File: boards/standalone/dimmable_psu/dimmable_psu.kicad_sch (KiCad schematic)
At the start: 81 parts, among them J1 DIM_IN, J2 PWM_IN, J3 POWER, J4 POWER_OUT, Q1 2N7002, Q2 IRF540N, Q3 IRF540N, SW1 SW_DIP_SPLIT_x02, U1 LM324, U2 LMC7660, U3 TPS92640

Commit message: rework dimmable_psu opamp power supplies
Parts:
- removed D1, D2, D3, D4: D_Schottky_Trans, Diode_SMD:D_SOD-123, symbol Device:D_Schottky
- removed D6: 15v, Diode_THT:D_DO-15_P12.70mm_Horizontal, symbol Device:D_Zener
- removed D9: 2.7v, Diode_THT:D_DO-15_P12.70mm_Horizontal, symbol Device:D_Zener
- removed U3: TPS92640, Package_SO:HTSSOP-14-1EP_4.4x5mm_P0.65mm_EP3.4x5mm_Mask3x3.1mm, symbol ti_reg:TPS92640
- added C4, C5: 100n, Capacitor_SMD:C_0805_2012Metric_Pad1.18x1.45mm_HandSolder, symbol Device:C
- added D1, D2: BAT54S, Package_TO_SOT_SMD:SOT-23, symbol Diode:BAT54S
- added R17: 47k, Resistor_SMD:R_0805_2012Metric_Pad1.20x1.40mm_HandSolder, symbol Device:R
- added R21: 59k, Resistor_SMD:R_0805_2012Metric_Pad1.20x1.40mm_HandSolder, symbol Device:R
- added U2: AP2205-ADJ, Package_TO_SOT_SMD:SOT-23-5, symbol Regulator_Linear:AP2204K-ADJ
- added U3: MAX17651, Package_TO_SOT_SMD:TSOT-23-6, symbol reg:MAX17651
- added U5: TPS92640, Package_SO:HTSSOP-14-1EP_4.4x5mm_P0.65mm_EP3.4x5mm_Mask3x3.1mm, symbol reg:TPS92640
- R16: value 1.2k -> 47k; footprint Resistor_THT:R_Axial_DIN0309_L9.0mm_D3.2mm_P12.70mm_Horizontal -> Resistor_SMD:R_0805_2012Metric_Pad1.20x1.40mm_HandSolder
- R2: renamed from R1; value 47k -> 22k
- R20: renamed from R8; value 750 -> 1.5M; footprint Resistor_THT:R_Axial_DIN0309_L9.0mm_D3.2mm_P12.70mm_Horizontal -> Resistor_SMD:R_0805_2012Metric_Pad1.20x1.40mm_HandSolder
- renumbered C2 to C1, C9 to C10, C10 to C11, C5 to C12, C11 to C13, C12 to C14, C13 to C15, C14 to C16, C15 to C17, C16 to C18, C17 to C19, C3 to C2, C18 to C20, C1 to C3, C4 to C9, D5 to D3, D7 to D4, D8 to D5, D10 to D6, R29 to R1, R17 to R18, R18 to R19, R19 to R22, R20 to R23, R21 to R24, R22 to R25, R23 to R26, R24 to R27, R25 to R28, R26 to R29, R2 to R3, R27 to R30, R28 to R31, R3 to R4, R4 to R5, R5 to R6, R6 to R7, R7 to R8, TP5 to TP4, TP6 to TP5, TP4 to TP6, U2 to U4
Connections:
- net CSENSE: now also U5.9 (CSENSE)
- net DIM_IN: now also D1.3
- net GND: now also C4.2, C5.2, D1.1, D2.1, R17.2, R21.2, U2.2 (GND), U3.2 (GND), U5.15 (TP), U5.8 (GND)
- net IADJ: now also U5.6 (IADJ)
- net POWER_JUN: now also U5.13 (SW)
- net PWM_IN: now also D2.3
- net UDIM: now also U5.3 (UDIM)
- net VDD: now also R20.1, C4.1, D1.2, D2.2, U2.1 (VIN), U2.3 (EN), U3.4 (OUT); no longer R20.2
- net VNEGREF: now also R16.1, U2.5 (VOUT); no longer R16.2
- net VOUT_SENSE: now also U5.4 (VOUT)
- net VPP: now also C5.1, U3.1 (EN), U3.3 (VIN), U5.1 (VIN); no longer R16.1, R20.1
- net VREF: now also U5.5 (VREF)
- net at R26.1: now also U5.10 (LG)
- net at C19.1, D6.2 (A): now also U5.11 (VCC)
- net at C18.2, D6.1 (K): now also U5.12 (BOOT)
- net at R25.1: now also U5.14 (HG)
- net at C13.1, R24.2: now also U5.2 (RON)
- net at C16.1: now also U5.7 (COMP)
- new net: R20.2, R21.1, U3.6 (FB)
- new net: R16.2, R17.1, U2.4 (ADJ)
- no-connect marks 4 -> 5
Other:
- moved on the sheet: C1, C12, C2, C6, C7, C9, R20, TP6

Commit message: dimmable psu pcb almost finished
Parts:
- added C3, C?: 100n, Capacitor_SMD:C_0805_2012Metric_Pad1.18x1.45mm_HandSolder, symbol Device:C
- renumbered C9 to C10, C10 to C11, C11 to C12, C12 to C13, C13 to C14, C14 to C15, C15 to C16, C16 to C17, C17 to C18, C18 to C19, C19 to C20, C20 to C21, C3 to C4, C4 to C5, C5 to C6, C6 to C7, C7 to C8, C8 to C9
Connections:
- net GND: now also C3.2, C?.2
- net UDIM: no longer TP5.1
- net UDIM_OFF: now also TP5.1
- net VDD: now also C?.1
- net VPP: now also C3.1
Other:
- moved on the sheet: TP5

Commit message: add filled areas and make some cosmetic fixes
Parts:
- gave numbers to parts that had none: 1
- renumbered C9 to C10, C10 to C11, C11 to C12, C12 to C13, C13 to C14, C14 to C15, C15 to C16, C16 to C17, C17 to C18, C18 to C19, C19 to C20, C20 to C21, C21 to C22, C4 to C5, C5 to C6, C6 to C7, C7 to C8, C8 to C9, TP5 to TP4, TP4 to TP5

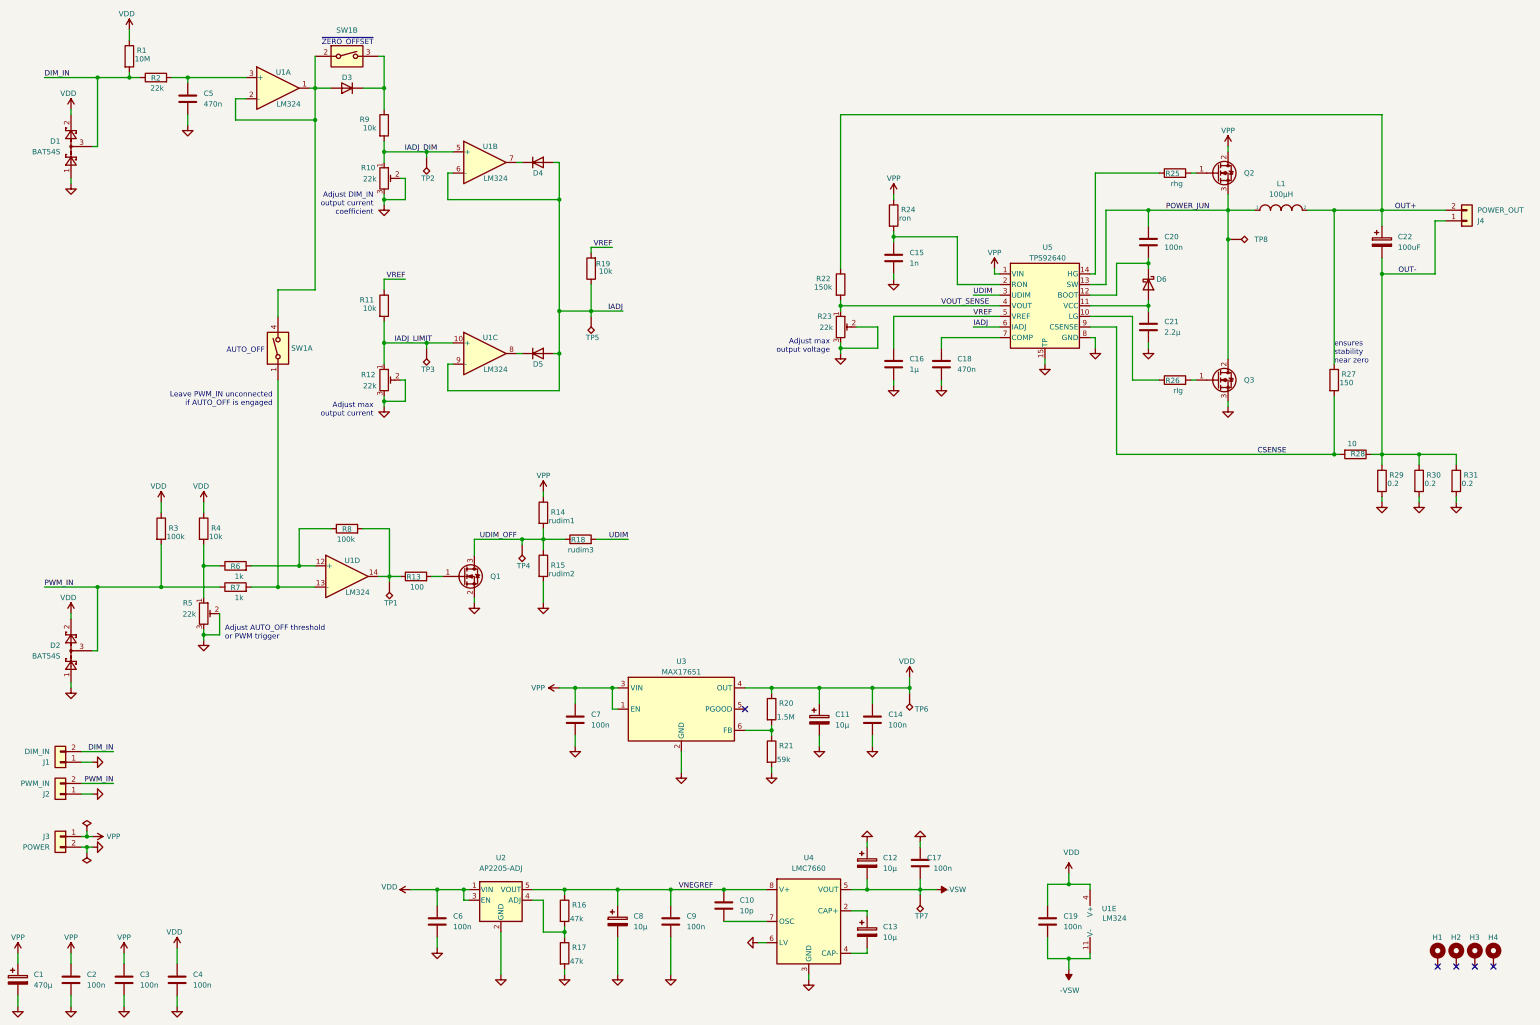
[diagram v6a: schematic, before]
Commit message: replace LDOs with npns
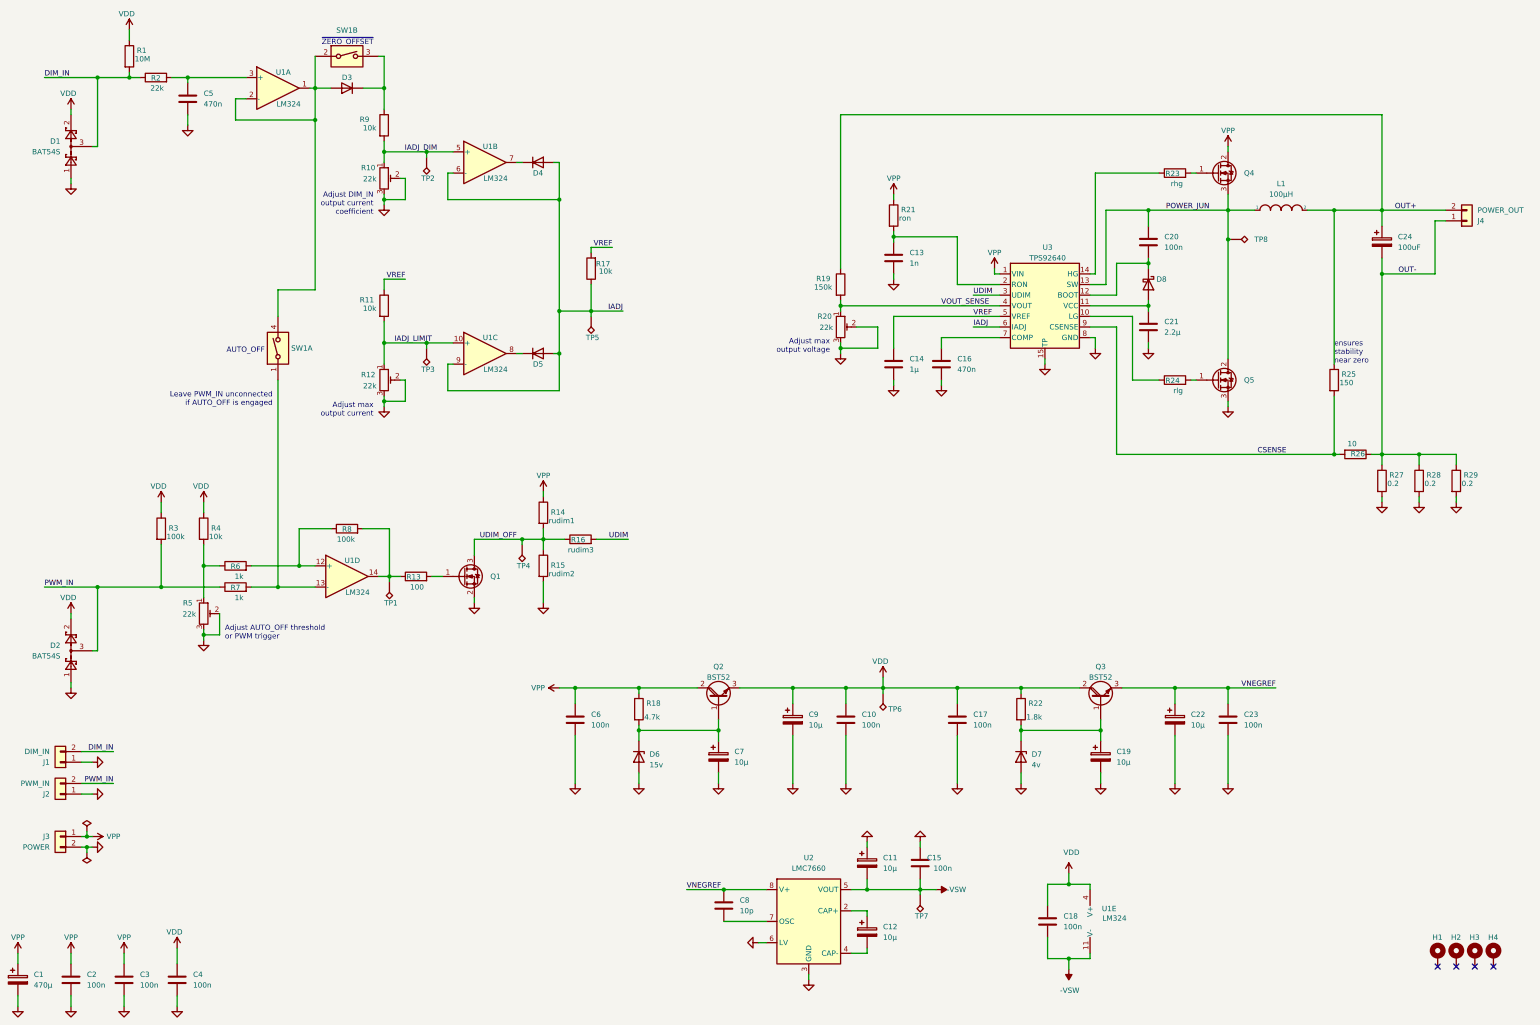
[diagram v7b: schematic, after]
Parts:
- removed C13, C8: 10µ, Capacitor_SMD:CP_Elec_5x5.4, symbol Device:C_Polarized
- removed C6, C9: 100n, Capacitor_SMD:C_0805_2012Metric_Pad1.18x1.45mm_HandSolder, symbol Device:C
- removed R16, R17: 47k, Resistor_SMD:R_0805_2012Metric_Pad1.20x1.40mm_HandSolder, symbol Device:R
- removed R20: 1.5M, Resistor_SMD:R_0805_2012Metric_Pad1.20x1.40mm_HandSolder, symbol Device:R
- removed R21: 59k, Resistor_SMD:R_0805_2012Metric_Pad1.20x1.40mm_HandSolder, symbol Device:R
- removed U2: AP2205-ADJ, Package_TO_SOT_SMD:SOT-23-5, symbol Regulator_Linear:AP2204K-ADJ
- removed U3: MAX17651, Package_TO_SOT_SMD:TSOT-23-6, symbol reg:MAX17651
- added C17, C23: 100n, Capacitor_SMD:C_0805_2012Metric_Pad1.18x1.45mm_HandSolder, symbol Device:C
- added C19, C22, C7, C9: 10µ, Capacitor_SMD:C_1206_3216Metric_Pad1.33x1.80mm_HandSolder, symbol Device:C_Polarized
- added D6: 15v, Diode_SMD:D_SOD-323_HandSoldering, symbol Device:D_Zener
- added D7: 4v, Diode_SMD:D_SOD-323_HandSoldering, symbol Device:D_Zener
- added Q2, Q3: BST52, Package_TO_SOT_SMD:SOT-89-3, symbol Transistor_BJT:BCV49
- added R18: 4.7k, Resistor_SMD:R_0805_2012Metric_Pad1.20x1.40mm_HandSolder, symbol Device:R
- added R22: 1.8k, Resistor_SMD:R_0805_2012Metric_Pad1.20x1.40mm_HandSolder, symbol Device:R
- C11, C12: footprint Capacitor_SMD:CP_Elec_5x5.4 -> Capacitor_SMD:C_1206_3216Metric_Pad1.33x1.80mm_HandSolder; shop https://store.comet.bg/Catalogue/Product/29567/ -> https://store.comet.bg/Catalogue/Product/5162150/
- renumbered C14 to C10, C15 to C13, C16 to C14, C17 to C15, C18 to C16, C19 to C18, C22 to C24, C7 to C6, C10 to C8, D6 to D8, Q2 to Q4, Q3 to Q5, R18 to R16, R19 to R17, R22 to R19, R23 to R20, R24 to R21, R25 to R23, R26 to R24, R27 to R25, R28 to R26, R29 to R27, R30 to R28, R31 to R29, U4 to U2, U5 to U3
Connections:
- net -VSW: now also C11.2; no longer C12.2
- net GND: now also C11.1, C17.2, C19.2, C22.2, C23.2, C7.2, C9.2, D6.2 (A), D7.2 (A); no longer C11.2, C12.1
- net VDD: now also C17.1, C9.1, Q2.3 (E), Q3.2 (C), R22.1; no longer C11.1
- net VNEGREF: now also C22.1, C23.1, Q3.3 (E)
- net VPP: now also Q2.2 (C), R18.1
- net at U2.2 (CAP+): now also C12.1
- net at U2.4 (CAP-): now also C12.2
- new net: C19.1, D7.1 (K), Q3.1 (B), R22.2
- new net: C7.1, D6.1 (K), Q2.1 (B), R18.2
- no-connect marks 5 -> 4
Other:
- moved on the sheet: C10, TP6

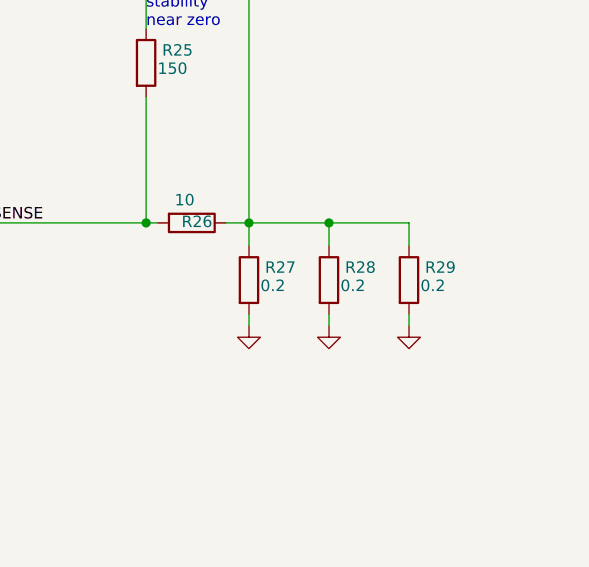
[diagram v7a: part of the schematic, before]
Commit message: use 1206 power resistors
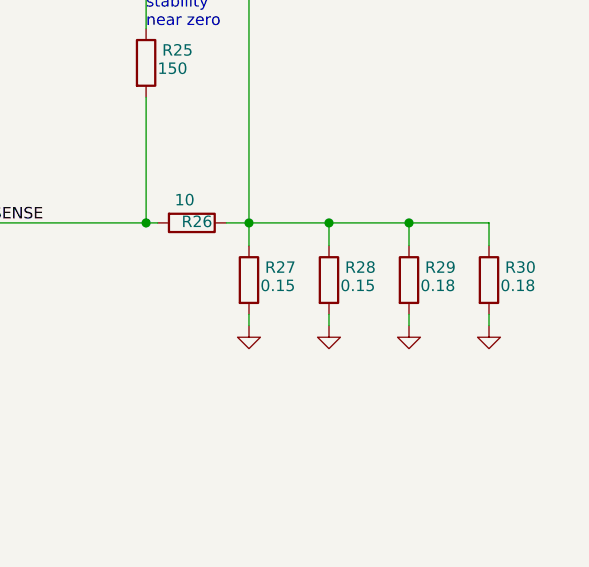
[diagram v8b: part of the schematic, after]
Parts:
- added R30: 0.18, Resistor_SMD:R_1206_3216Metric_Pad1.30x1.75mm_HandSolder, symbol Device:R
- R25, R26: footprint Resistor_THT:R_Axial_DIN0309_L9.0mm_D3.2mm_P12.70mm_Horizontal -> Resistor_SMD:R_1206_3216Metric_Pad1.30x1.75mm_HandSolder
- R27, R28: value 0.2 -> 0.15; footprint Resistor_THT:R_Axial_DIN0309_L9.0mm_D3.2mm_P12.70mm_Horizontal -> Resistor_SMD:R_1206_3216Metric_Pad1.30x1.75mm_HandSolder
- R29: value 0.2 -> 0.18; footprint Resistor_THT:R_Axial_DIN0309_L9.0mm_D3.2mm_P12.70mm_Horizontal -> Resistor_SMD:R_1206_3216Metric_Pad1.30x1.75mm_HandSolder
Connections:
- net GND: now also R30.2
- net OUT-: now also R30.1
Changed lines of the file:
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@@
-(kicad_sch (version 20210126) (generator eeschema)
+(kicad_sch (version 20210406) (generator eeschema)
   (paper "A3")
   (title_block
@@
   (junction (at 359.41 135.89) (diameter 1.016) (color 0 0 0 0))
   (junction (at 368.3 135.89) (diameter 1.016) (color 0 0 0 0))
+  (junction (at 377.19 135.89) (diameter 1.016) (color 0 0 0 0))
   (no_connect (at 372.745 258.445))
   (no_connect (at 377.19 258.445))
@@
     (stroke (width 0) (type solid) (color 0 0 0 0))
   )
+  (wire (pts (xy 386.08 135.89) (xy 377.19 135.89))
+    (stroke (width 0) (type solid) (color 0 0 0 0))
+  )
+  (wire (pts (xy 386.08 138.43) (xy 386.08 135.89))
+    (stroke (width 0) (type solid) (color 0 0 0 0))
+  )
+  (wire (pts (xy 386.08 146.05) (xy 386.08 147.32))
+    (stroke (width 0) (type solid) (color 0 0 0 0))
+  )
   (text "Adjust AUTO_OFF threshold\nor PWM trigger" (at 82.55 180.34 0)
     (effects (font (size 1.27 1.27)) (justify left bottom))
@@
     (pin "1")
   )
+  (symbol (lib_id "power:GND") (at 386.08 147.32 0) (unit 1)
+    (in_bom yes) (on_board yes)
+    (property "Reference" "#PWR060" (id 0) (at 386.08 153.67 0)
+      (effects (font (size 1.27 1.27)) hide)
+    )
+    (property "Value" "GND" (id 1) (at 386.715 152.4 0)
+      (effects (font (size 1.27 1.27)) hide)
+    )
+    (property "Footprint" "" (id 2) (at 386.08 147.32 0)
+      (effects (font (size 1.27 1.27)) hide)
+    )
+    (property "Datasheet" "" (id 3) (at 386.08 147.32 0)
+      (effects (font (size 1.27 1.27)) hide)
+    )
+    (pin "1")
+  )
   (symbol (lib_id "Amplifier_Operational:LM324") (at 292.1 247.65 0) (unit 5)
     (in_bom yes) (on_board yes)
@@
       (effects (font (size 1.27 1.27)) (justify left))
     )
-    (property "Footprint" "Resistor_THT:R_Axial_DIN0309_L9.0mm_D3.2mm_P12.70mm_Horizontal" (id 2) (at 346.202 118.11 90)
+    (property "Footprint" "Resistor_SMD:R_1206_3216Metric_Pad1.30x1.75mm_HandSolder" (id 2) (at 346.202 118.11 90)
       (effects (font (size 1.27 1.27)) hide)
     )
@@
       (effects (font (size 1.27 1.27)) (justify left))
     )
-    (property "Footprint" "Resistor_THT:R_Axial_DIN0309_L9.0mm_D3.2mm_P12.70mm_Horizontal" (id 2) (at 353.06 134.112 90)
+    (property "Footprint" "Resistor_SMD:R_1206_3216Metric_Pad1.30x1.75mm_HandSolder" (id 2) (at 353.06 134.112 90)
       (effects (font (size 1.27 1.27)) hide)
     )
@@
       (effects (font (size 1.27 1.27)) (justify left))
     )
-    (property "Value" "0.2" (id 1) (at 360.68 142.875 0)
+    (property "Value" "0.15" (id 1) (at 360.68 142.875 0)
       (effects (font (size 1.27 1.27)) (justify left))
     )
-    (property "Footprint" "Resistor_THT:R_Axial_DIN0309_L9.0mm_D3.2mm_P12.70mm_Horizontal" (id 2) (at 357.632 142.24 90)
+    (property "Footprint" "Resistor_SMD:R_1206_3216Metric_Pad1.30x1.75mm_HandSolder" (id 2) (at 357.632 142.24 90)
       (effects (font (size 1.27 1.27)) hide)
     )
@@
       (effects (font (size 1.27 1.27)) (justify left))
     )
-    (property "Value" "0.2" (id 1) (at 369.57 142.875 0)
+    (property "Value" "0.15" (id 1) (at 369.57 142.875 0)
       (effects (font (size 1.27 1.27)) (justify left))
     )
-    (property "Footprint" "Resistor_THT:R_Axial_DIN0309_L9.0mm_D3.2mm_P12.70mm_Horizontal" (id 2) (at 366.522 142.24 90)
+    (property "Footprint" "Resistor_SMD:R_1206_3216Metric_Pad1.30x1.75mm_HandSolder" (id 2) (at 366.522 142.24 90)
       (effects (font (size 1.27 1.27)) hide)
     )
@@
       (effects (font (size 1.27 1.27)) (justify left))
     )
-    (property "Value" "0.2" (id 1) (at 378.46 142.875 0)
+    (property "Value" "0.18" (id 1) (at 378.46 142.875 0)
       (effects (font (size 1.27 1.27)) (justify left))
     )
-    (property "Footprint" "Resistor_THT:R_Axial_DIN0309_L9.0mm_D3.2mm_P12.70mm_Horizontal" (id 2) (at 375.412 142.24 90)
+    (property "Footprint" "Resistor_SMD:R_1206_3216Metric_Pad1.30x1.75mm_HandSolder" (id 2) (at 375.412 142.24 90)
       (effects (font (size 1.27 1.27)) hide)
     )
@@
     (pin "2")
   )
+  (symbol (lib_id "Device:R") (at 386.08 142.24 0) (unit 1)
+    (in_bom yes) (on_board yes)
+    (property "Reference" "R30" (id 0) (at 387.858 140.843 0)
+      (effects (font (size 1.27 1.27)) (justify left))
+    )
+    (property "Value" "0.18" (id 1) (at 387.35 142.875 0)
+      (effects (font (size 1.27 1.27)) (justify left))
+    )
+    (property "Footprint" "Resistor_SMD:R_1206_3216Metric_Pad1.30x1.75mm_HandSolder" (id 2) (at 384.302 142.24 90)
+      (effects (font (size 1.27 1.27)) hide)
+    )
+    (property "Datasheet" "~" (id 3) (at 386.08 142.24 0)
+      (effects (font (size 1.27 1.27)) hide)
+    )
+    (pin "1")
+    (pin "2")
+  )
   (symbol (lib_id "pspice:INDUCTOR") (at 335.28 77.47 0) (unit 1)
     (in_bom yes) (on_board yes)
@@
       (reference "#PWR059") (unit 1) (value "GND") (footprint "")
     )
+    (path "/86498e4e-c4a8-4e93-bbda-f02af6283b6c"
+      (reference "#PWR060") (unit 1) (value "GND") (footprint "")
+    )
     (path "/2e5255b4-943c-4c3c-88ee-e6eaf46dc6bd"
       (reference "C1") (unit 1) (value "470µ") (footprint "Capacitor_THT:CP_Radial_D16.0mm_P7.50mm")
@@
     )
     (path "/1ee19456-ad1e-4a58-83dc-99b7d865cfbd"
-      (reference "R25") (unit 1) (value "150") (footprint "Resistor_THT:R_Axial_DIN0309_L9.0mm_D3.2mm_P12.70mm_Horizontal")
+      (reference "R25") (unit 1) (value "150") (footprint "Resistor_SMD:R_1206_3216Metric_Pad1.30x1.75mm_HandSolder")
     )
     (path "/9831014f-957a-4e2f-ad6a-bac7575e5ac9"
-      (reference "R26") (unit 1) (value "10") (footprint "Resistor_THT:R_Axial_DIN0309_L9.0mm_D3.2mm_P12.70mm_Horizontal")
+      (reference "R26") (unit 1) (value "10") (footprint "Resistor_SMD:R_1206_3216Metric_Pad1.30x1.75mm_HandSolder")
     )
     (path "/dfc0f561-c7b2-4435-a893-5b08b0cf2f7c"
-      (reference "R27") (unit 1) (value "0.2") (footprint "Resistor_THT:R_Axial_DIN0309_L9.0mm_D3.2mm_P12.70mm_Horizontal")
+      (reference "R27") (unit 1) (value "0.15") (footprint "Resistor_SMD:R_1206_3216Metric_Pad1.30x1.75mm_HandSolder")
     )
     (path "/2ce0e720-7616-44e7-a612-f46846fe4849"
-      (reference "R28") (unit 1) (value "0.2") (footprint "Resistor_THT:R_Axial_DIN0309_L9.0mm_D3.2mm_P12.70mm_Horizontal")
+      (reference "R28") (unit 1) (value "0.15") (footprint "Resistor_SMD:R_1206_3216Metric_Pad1.30x1.75mm_HandSolder")
     )
     (path "/8cb73d3a-34e5-4fed-bc36-e3e5a0fb05ef"
-      (reference "R29") (unit 1) (value "0.2") (footprint "Resistor_THT:R_Axial_DIN0309_L9.0mm_D3.2mm_P12.70mm_Horizontal")
+      (reference "R29") (unit 1) (value "0.18") (footprint "Resistor_SMD:R_1206_3216Metric_Pad1.30x1.75mm_HandSolder")
+    )
+    (path "/56e1feac-8458-43fd-ab79-d039abd4ffc0"
+      (reference "R30") (unit 1) (value "0.18") (footprint "Resistor_SMD:R_1206_3216Metric_Pad1.30x1.75mm_HandSolder")
     )
     (path "/5cb36b70-e933-4478-a32f-7d281ff0571f"
